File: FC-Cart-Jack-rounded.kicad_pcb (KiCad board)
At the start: 2 copper layers, 90 x 56.8 mm, 4 parts, among them J1 ToCartridge, J2 ToConsole

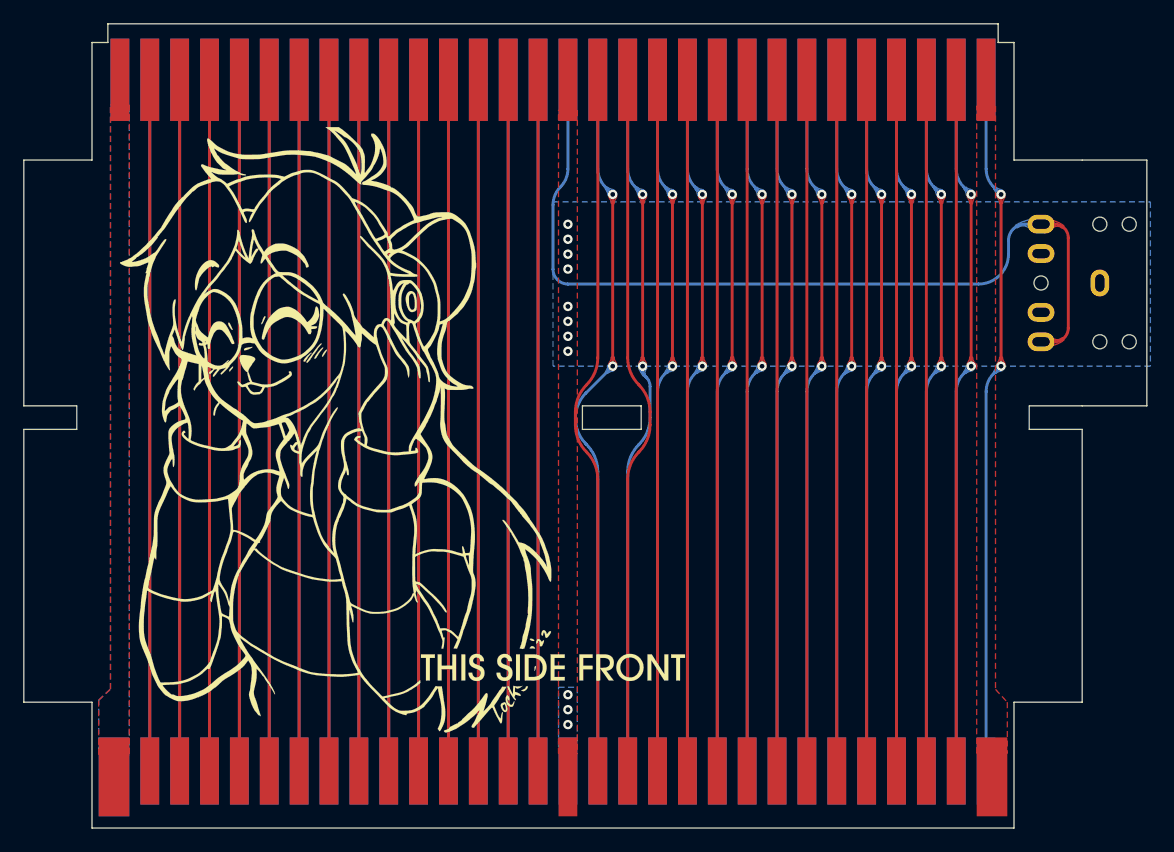
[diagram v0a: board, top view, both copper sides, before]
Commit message: Leave audio out floating
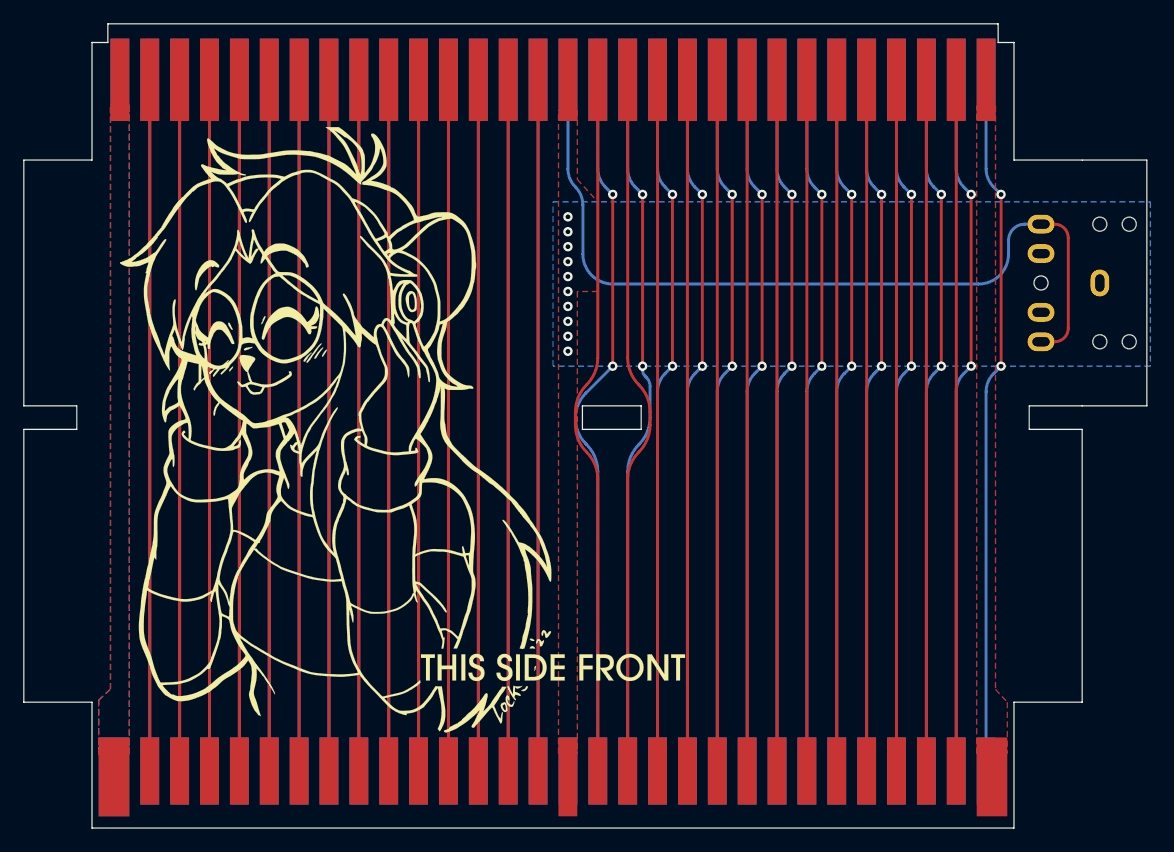
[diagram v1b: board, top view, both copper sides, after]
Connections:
- net /AUD_From2A03 renamed /AUD_2A03
- J2 pad 46: GND -> unconnected-(J2-Pad46)
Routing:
- net /AUD_Output: track 75.4 -> 72.2 mm
- net GND: vias 11 -> 10

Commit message: Optionally terminate audio with 100K resistor
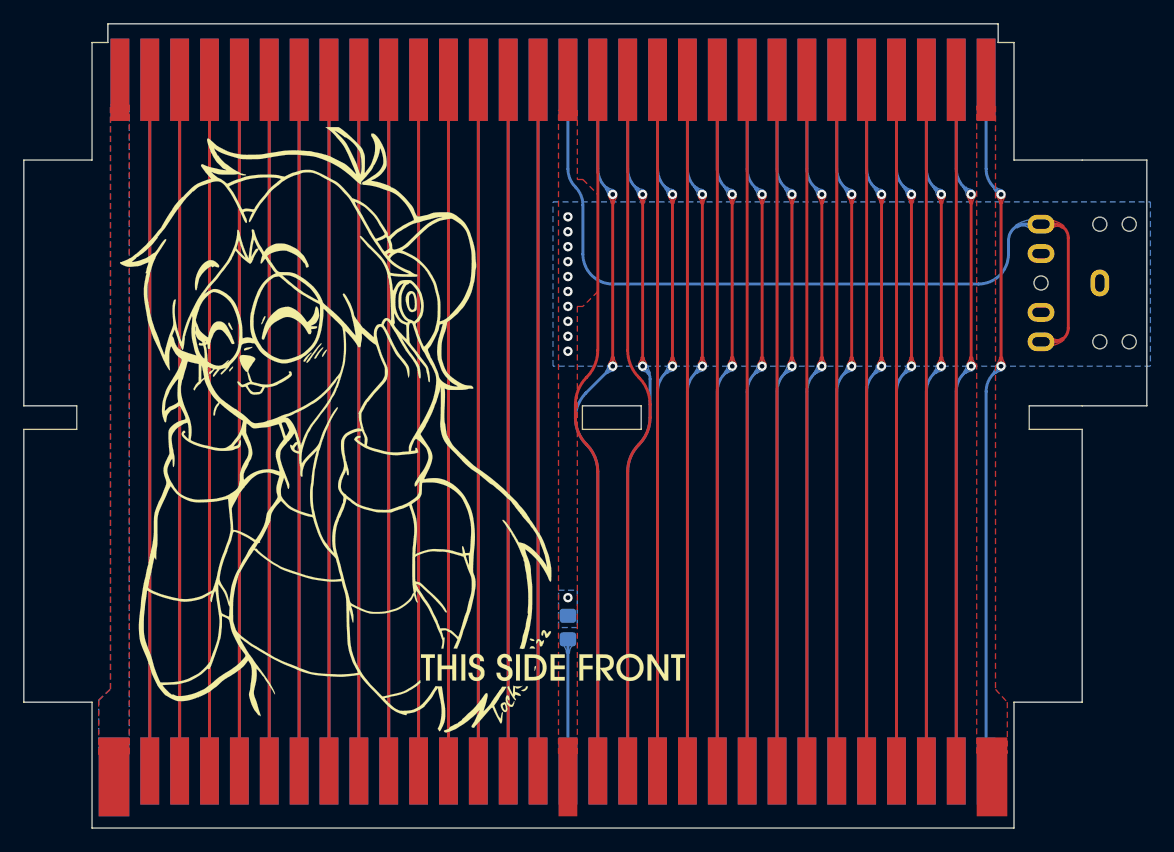
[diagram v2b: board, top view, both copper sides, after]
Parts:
- added R1: 100K, Resistor_SMD:R_0805_2012Metric_Pad1.20x1.40mm_HandSolder, B.Cu at (128.3, 120.7)
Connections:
- J2 pad 46: unconnected-(J2-Pad46) -> /AUD_RF
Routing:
- net /AUD_RF: track 0.00 -> 11.2 mm
- net GND: vias 10 -> 11
